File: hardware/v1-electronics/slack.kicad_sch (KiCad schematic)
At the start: 0 parts

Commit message: refactor(v1 hardware): led matrix now uses hierarchical labels
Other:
- sheet LED Matrix ports: added CS10_1, CS10_2, CS11_1, CS11_2, CS12_1, CS12_2, CS13_1, CS13_2, CS14_1, CS14_2, CS15_1, CS15_2, CS16_1, CS16_2, CS1_1, CS1_2, CS2_1, CS2_2, CS3_1, CS3_2, CS4_1, CS4_2, CS5_1, CS5_2, CS6_1, CS6_2, CS7_1, CS7_2, CS8_1, CS8_2, CS9_1, CS9_2, SW10_G_1, SW10_G_2, SW11_R_1, SW11_R_2, SW12_W_1, SW12_W_2, SW1_B_1, SW1_B_2, SW2_G_1, SW2_G_2, SW3_R_1, SW3_R_2, SW4_W_1, SW4_W_2, SW5_B_1, SW5_B_2, SW6_G_1, SW6_G_2, SW7_R_1, SW7_R_2, SW8_W_1, SW8_W_2, SW9_B_1, SW9_B_2; removed none

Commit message: refactor(v1 hardware): all sheets now use hierarchical labels
We'll might change these to buses down the line, but we'll see
I'm happy for now
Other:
- sheet LED Matrix renamed LED Matricies
- sheet Controller ICs ports: added CS10_1, CS10_2, CS11_1, CS11_2, CS12_1, CS12_2, CS13_1, CS13_2, CS14_1, CS14_2, CS15_1, CS15_2, CS16_1, CS16_2, CS1_1, CS1_2, CS2_1, CS2_2, CS3_1, CS3_2, CS4_1, CS4_2, CS5_1, CS5_2, CS6_1, CS6_2, CS7_1, CS7_2, CS8_1, CS8_2, CS9_1, CS9_2, Column 1, Column 10, Column 11, Column 12, Column 13, Column 14, Column 2, Column 3, Column 4, Column 5, Column 6, Column 7, Column 8, Column 9, D+, D-, I2C1_SCL, I2C1_SDA, RE10_A-Channel, RE10_B-Channel, RE1_A-Channel, RE1_B-Channel, RE2_A-Channel, RE2_B-Channel, RE3_A-Channel, RE3_B-Channel, RE4_A-Channel, RE4_B-Channel, RE5_A-Channel, RE5_B-Channel, RE6_A-Channel, RE6_B-Channel, RE7_A-Channel, RE7_B-Channel, RE8_A-Channel, RE8_B-Channel, RE9_A-Channel, RE9_B-Channel, Row 1, Row 2, Row 3, Row 4, Row 5, Row 6, SW10_G_1, SW10_G_2, SW11_R_1, SW11_R_2, SW12_W_1, SW12_W_2, SW1_B_1, SW1_B_2, SW2_G_1, SW2_G_2, SW3_R_1, SW3_R_2, SW4_W_1, SW4_W_2, SW5_B_1, SW5_B_2, SW6_G_1, SW6_G_2, SW7_R_1, SW7_R_2, SW8_W_1, SW8_W_2, SW9_B_1, SW9_B_2, TPS61288_EN, ~{MP2721_INT}; removed none
- sheet Power Train ports: added I2C1_SCL, I2C1_SDA, TPS61288_EN, ~{MP2721_INT}; removed VBUS, V_SYS
- note added: "- Compare charger ICs - Check circuits - Choose passive conponent values - Connect the LED and Switch matrices. Assign LEDs to each inputs. - Select PCB foot prints I feel that my power and ground levels are confusing Schematic - Refactor Schematic to r/PrintedCircuitBoard Guide - Refactor the root schematic to show how the system is connected - I want to add logic levels and ground differentiati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"
- note added: "KiCad Feature Requests: Hierarchical Bus Hierarchical Sheet Symbols"
- note removed: "- Compare charger ICs - Check circuits - Choose passive conponent values - Connect the LED and Switch matrices. Assign LEDs to each inputs. - Select PCB foot prints Schematic - Refactor Schematic to r/PrintedCircuitBoard Guide - Refactor the root schematic to show how the system is connected - Refactor chip configurations to explain my choices - Rename all the component references so they are gro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"

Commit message: refactor(v1 hardware): root level schematic is made discriptive with hierarchical pins
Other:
- sheet Controller ICs ports: added Chip1CurrentSource[1..16], Chip1SinkSwitch[1..12], Chip2CurrentSource[1..16], Chip2SinkSwitch[1..12], Column[1..14], I2C1{SDA, SCL}, RotaryEncoder_AChannel[1..10], RotaryEncoder_BChannel[1..10], Row[1..6], USB{D+, D-}; removed CS10_1, CS10_2, CS11_1, CS11_2, CS12_1, CS12_2, CS13_1, CS13_2, CS14_1, CS14_2, CS15_1, CS15_2, CS16_1, CS16_2, CS1_1, CS1_2, CS2_1, CS2_2, CS3_1, CS3_2, CS4_1, CS4_2, CS5_1, CS5_2, CS6_1, CS6_2, CS7_1, CS7_2, CS8_1, CS8_2, CS9_1, CS9_2, Column 1, Column 10, Column 11, Column 12, Column 13, Column 14, Column 2, Column 3, Column 4, Column 5, Column 6, Column 7, Column 8, Column 9, D+, D-, I2C1_SCL, I2C1_SDA, RE10_A-Channel, RE10_B-Channel, RE1_A-Channel, RE1_B-Channel, RE2_A-Channel, RE2_B-Channel, RE3_A-Channel, RE3_B-Channel, RE4_A-Channel, RE4_B-Channel, RE5_A-Channel, RE5_B-Channel, RE6_A-Channel, RE6_B-Channel, RE7_A-Channel, RE7_B-Channel, RE8_A-Channel, RE8_B-Channel, RE9_A-Channel, RE9_B-Channel, Row 1, Row 2, Row 3, Row 4, Row 5, Row 6, SW10_G_1, SW10_G_2, SW11_R_1, SW11_R_2, SW12_W_1, SW12_W_2, SW1_B_1, SW1_B_2, SW2_G_1, SW2_G_2, SW3_R_1, SW3_R_2, SW4_W_1, SW4_W_2, SW5_B_1, SW5_B_2, SW6_G_1, SW6_G_2, SW7_R_1, SW7_R_2, SW8_W_1, SW8_W_2, SW9_B_1, SW9_B_2
- sheet LED Matricies ports: added Chip1CurrentSource[1..16], Chip1SinkSwitch[1..12], Chip2CurrentSource[1..16], Chip2SinkSwitch[1..12]; removed CS10_1, CS10_2, CS11_1, CS11_2, CS12_1, CS12_2, CS13_1, CS13_2, CS14_1, CS14_2, CS15_1, CS15_2, CS16_1, CS16_2, CS1_1, CS1_2, CS2_1, CS2_2, CS3_1, CS3_2, CS4_1, CS4_2, CS5_1, CS5_2, CS6_1, CS6_2, CS7_1, CS7_2, CS8_1, CS8_2, CS9_1, CS9_2, SW10_G_1, SW10_G_2, SW11_R_1, SW11_R_2, SW12_W_1, SW12_W_2, SW1_B_1, SW1_B_2, SW2_G_1, SW2_G_2, SW3_R_1, SW3_R_2, SW4_W_1, SW4_W_2, SW5_B_1, SW5_B_2, SW6_G_1, SW6_G_2, SW7_R_1, SW7_R_2, SW8_W_1, SW8_W_2, SW9_B_1, SW9_B_2
- sheet Power Train ports: added I2C1{SDA, SCL}, USB{D+, D-}; removed D+, D-, I2C1_SCL, I2C1_SDA
- sheet Switch Matrix ports: added Column[1..14], RotaryEncoder_AChannel[1..10], RotaryEncoder_BChannel[1..10], Row[1..6]; removed Column 1, Column 10, Column 11, Column 12, Column 13, Column 14, Column 2, Column 3, Column 4, Column 5, Column 6, Column 7, Column 8, Column 9, RE10_A-Channel, RE10_B-Channel, RE1_A-Channel, RE1_B-Channel, RE2_A-Channel, RE2_B-Channel, RE3_A-Channel, RE3_B-Channel, RE4_A-Channel, RE4_B-Channel, RE5_A-Channel, RE5_B-Channel, RE6_A-Channel, RE6_B-Channel, RE7_A-Channel, RE7_B-Channel, RE8_A-Channel, RE8_B-Channel, RE9_A-Channel, RE9_B-Channel, Row 1, Row 2, Row 3, Row 4, Row 5, Row 6

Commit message: refactor(v1 hardware): refactored led controllers into a seperate sheet
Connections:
- no-connect marks 0 -> 6
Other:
- sheet Controller ICs renamed MCU
- sheet LED Matricies ports: added Chip1I2C_Reset, Chip1Interrupt, Chip1Shutdown, Chip2I2C_Reset, Chip2Interrupt, Chip2Shutdown, I2C1{SDA, SCL}; removed Chip1CurrentSource[1..16], Chip1SinkSwitch[1..12], Chip2CurrentSource[1..16], Chip2SinkSwitch[1..12]
- sheet MCU ports: added none; removed Chip1CurrentSource[1..16], Chip1SinkSwitch[1..12], Chip2CurrentSource[1..16], Chip2SinkSwitch[1..12]
- note added: "- Compare charger ICs - Check circuits - Choose passive conponent values - Connect the LED and Switch matrices. Assign LEDs to each inputs. - Select PCB foot prints I feel that my power and ground levels are confusing Schematic - Refactor Schematic to r/PrintedCircuitBoard Guide - [x] Refactor the root schematic to show how the system is connected - I want to add logic levels and ground different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"
- note removed: "- Compare charger ICs - Check circuits - Choose passive conponent values - Connect the LED and Switch matrices. Assign LEDs to each inputs. - Select PCB foot prints I feel that my power and ground levels are confusing Schematic - Refactor Schematic to r/PrintedCircuitBoard Guide - Refactor the root schematic to show how the system is connected - I want to add logic levels and ground differentiati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"

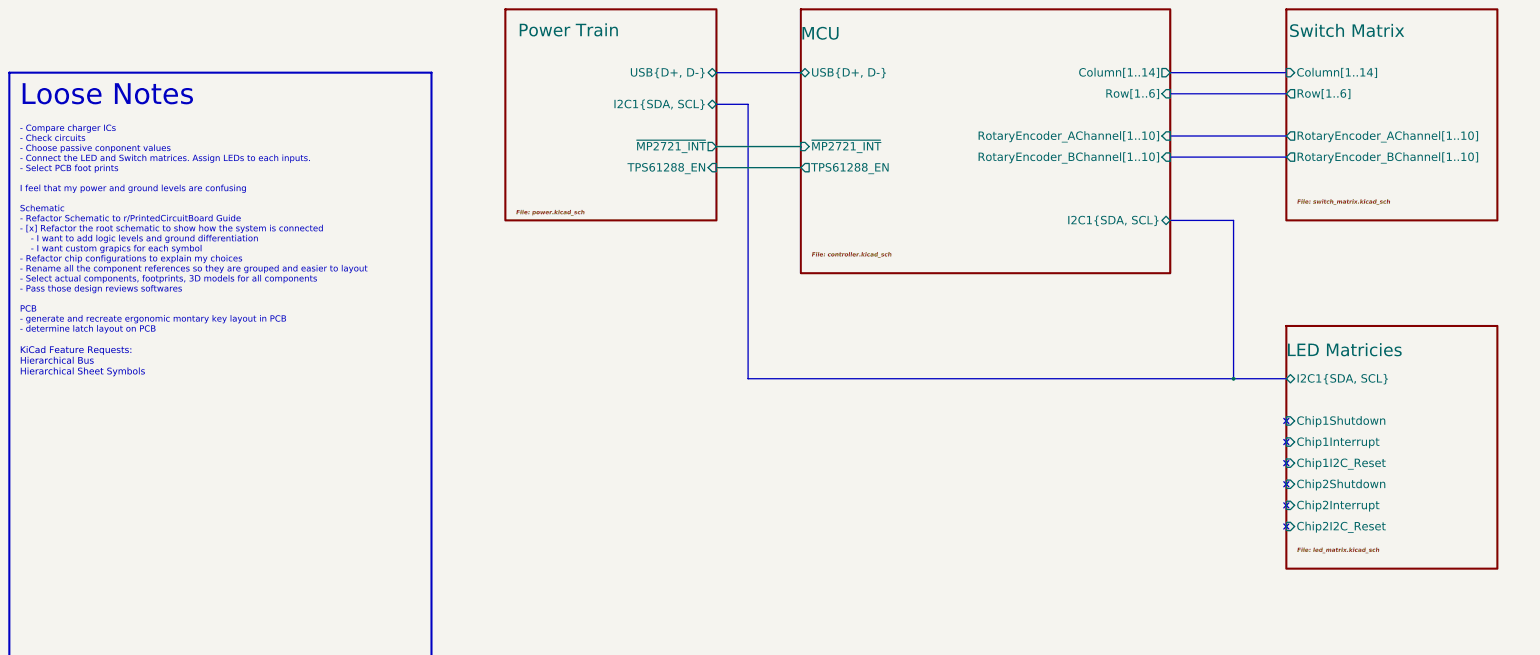
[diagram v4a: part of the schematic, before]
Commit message: refactor(v1 hardware): get references in order
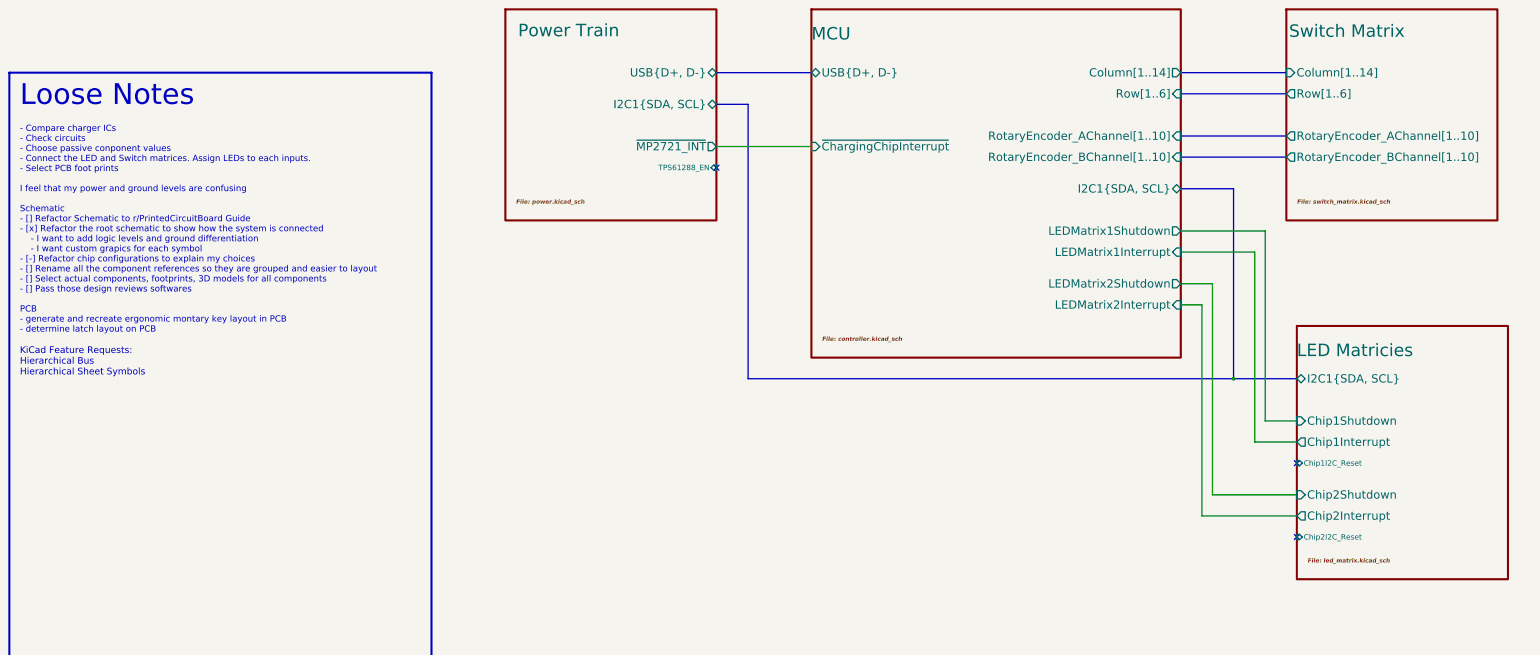
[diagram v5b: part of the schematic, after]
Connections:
- no-connect marks 6 -> 3
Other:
- sheet MCU ports: added LEDMatrix1Interrupt, LEDMatrix1Shutdown, LEDMatrix2Interrupt, LEDMatrix2Shutdown, ~{ChargingChipInterrupt}; removed TPS61288_EN, ~{MP2721_INT}
- note added: "- Compare charger ICs - Check circuits - Choose passive conponent values - Connect the LED and Switch matrices. Assign LEDs to each inputs. - Select PCB foot prints I feel that my power and ground levels are confusing Schematic - [] Refactor Schematic to r/PrintedCircuitBoard Guide - [x] Refactor the root schematic to show how the system is connected - I want to add logic levels and ground differ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"
- note removed: "- Compare charger ICs - Check circuits - Choose passive conponent values - Connect the LED and Switch matrices. Assign LEDs to each inputs. - Select PCB foot prints I feel that my power and ground levels are confusing Schematic - Refactor Schematic to r/PrintedCircuitBoard Guide - [x] Refactor the root schematic to show how the system is connected - I want to add logic levels and ground different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"
